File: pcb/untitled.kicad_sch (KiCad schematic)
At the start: 50 parts

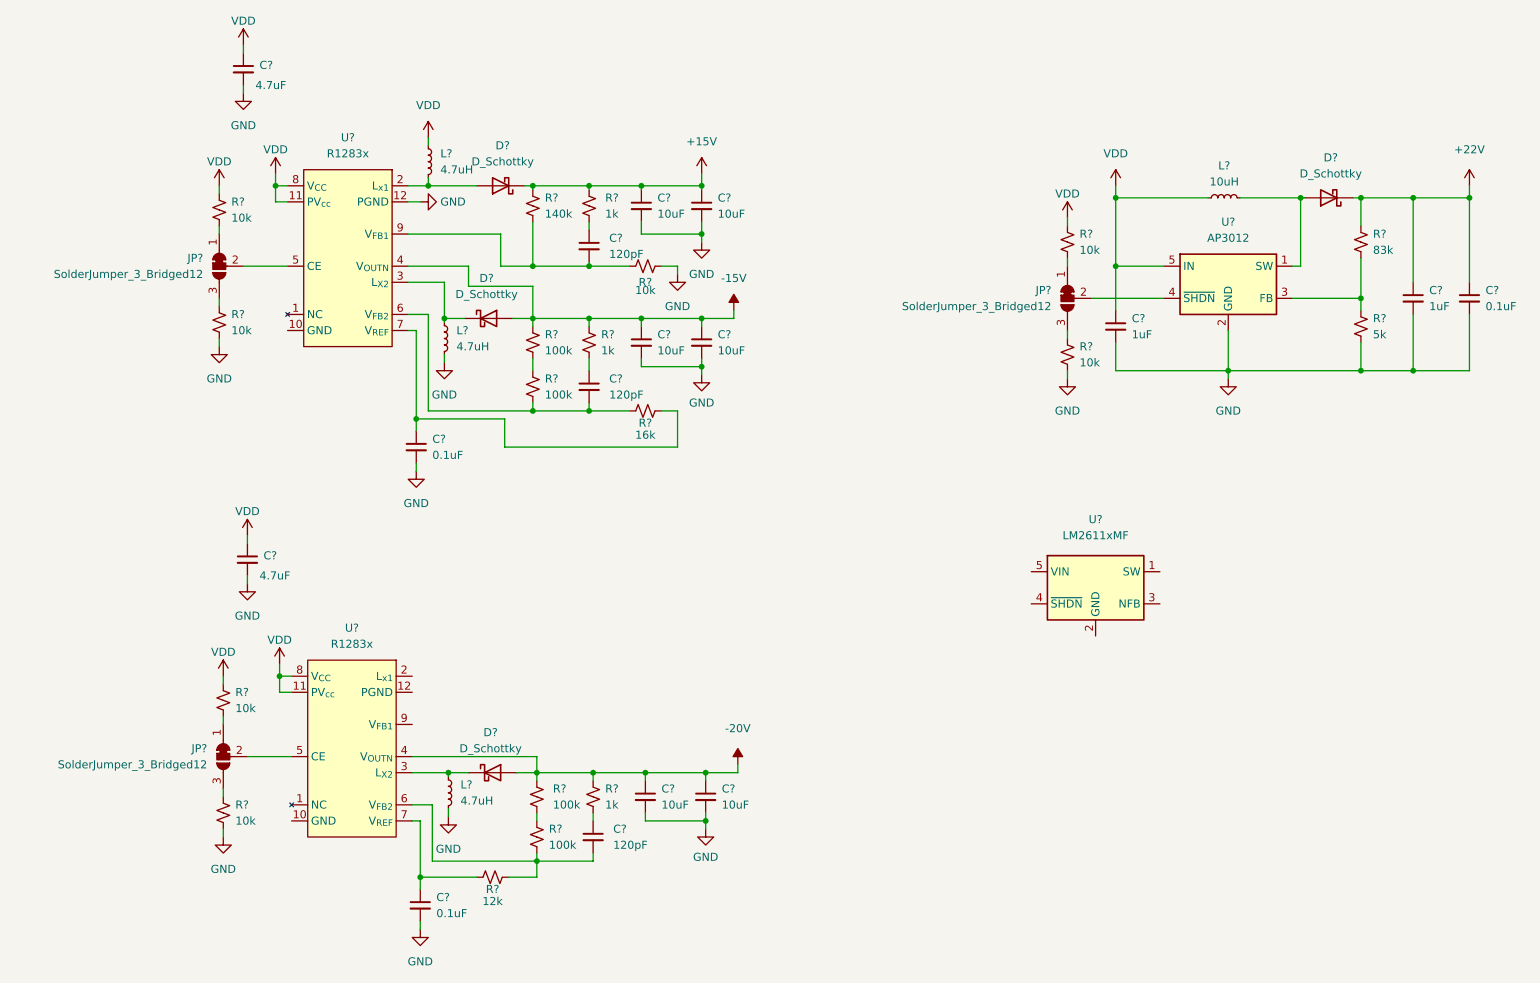
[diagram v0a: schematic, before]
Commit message: Tied physical components to layout components and created initial pcb file
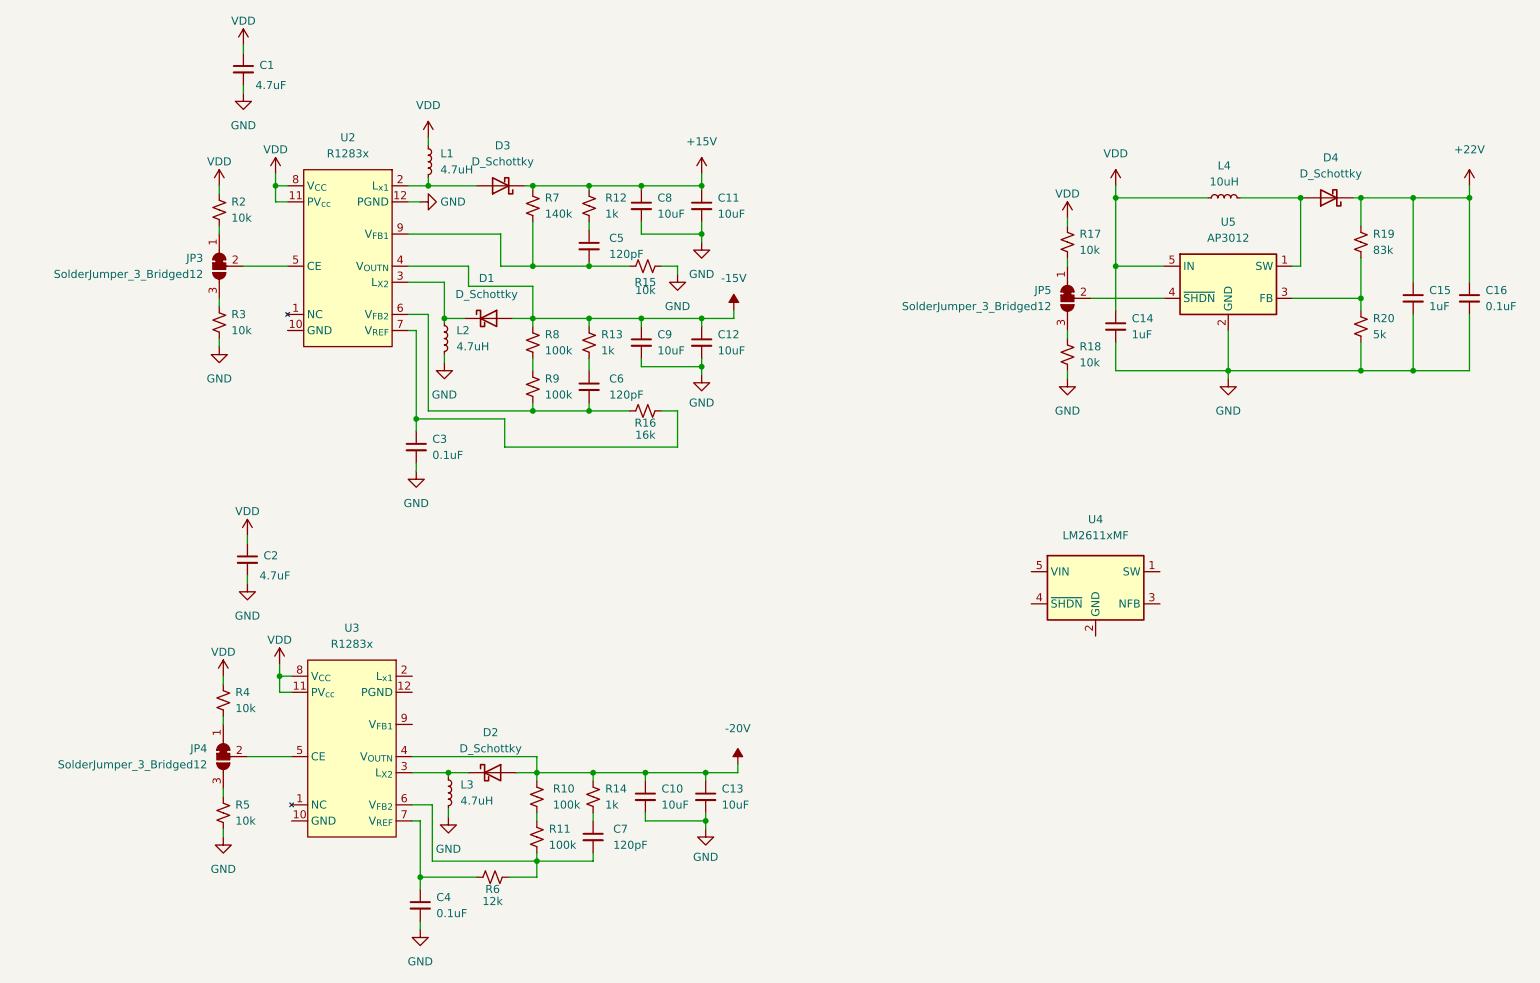
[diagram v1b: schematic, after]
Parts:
- JP3, JP4, JP5: renamed from JP?; footprint (none) -> Jumper:SolderJumper-3_P1.3mm_Bridged12_Pad1.0x1.5mm
- R10, R11, R12, R13, R14, R15, R16, R17, R18, R19, R2, R20, R3, R4, R5, R6, R7, R8, R9: renamed from R?; footprint (none) -> Resistor_SMD:R_0603_1608Metric
- gave numbers to parts that had none: 28
